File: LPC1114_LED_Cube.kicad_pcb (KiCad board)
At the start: 2 copper layers, 100 x 100 mm, 88 parts, among them Q201 BSS138, Q202 BSS138, Q203 BSS138, Q204 BSS138, Q205 IRLML6402TRPBF, Q206 IRLML6402TRPBF, Q207 IRLML6402TRPBF, Q208 IRLML6402TRPBF, Q209 BSS138, Q210 BSS138, Q211 BSS138, Q212 BSS138, Q213 IRLML6402TRPBF, Q214 IRLML6402TRPBF, Q215 IRLML6402TRPBF, Q216 IRLML6402TRPBF, Y101 12MHZ, Y102 12MHZ

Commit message: Completed Rev 1A
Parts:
- moved Q209 0.25 mm to (105.7, 74.5)
- moved Q201 0.25 mm to (90.4, 74.5)
- moved Q211 0.25 mm to (113.3, 74.5)
- moved C104 0.20 mm to (162.6, 99.9)
- moved Q212 0.13 mm to (115.1, 80.3)
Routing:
- net GND: track 92.4 -> 123.7 mm, vias 60 -> 63
- net TXD_USB: track 65.9 -> 69.3 mm
- net RXD_USB: track 65.9 -> 68.8 mm
- net LAYER_6_ON: track 63.6 -> 64.1 mm
- net Net-(LED_CH2_CTRL0-Pad27): track 7.54 -> 7.02 mm
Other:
- board text added: "0"
- board text added: "0.1uF"
- board text added: "15"
- board text added: "39pF"
- board text added: "56"
- board text added: "63"
- board text added: "7"
- board text added: "8"

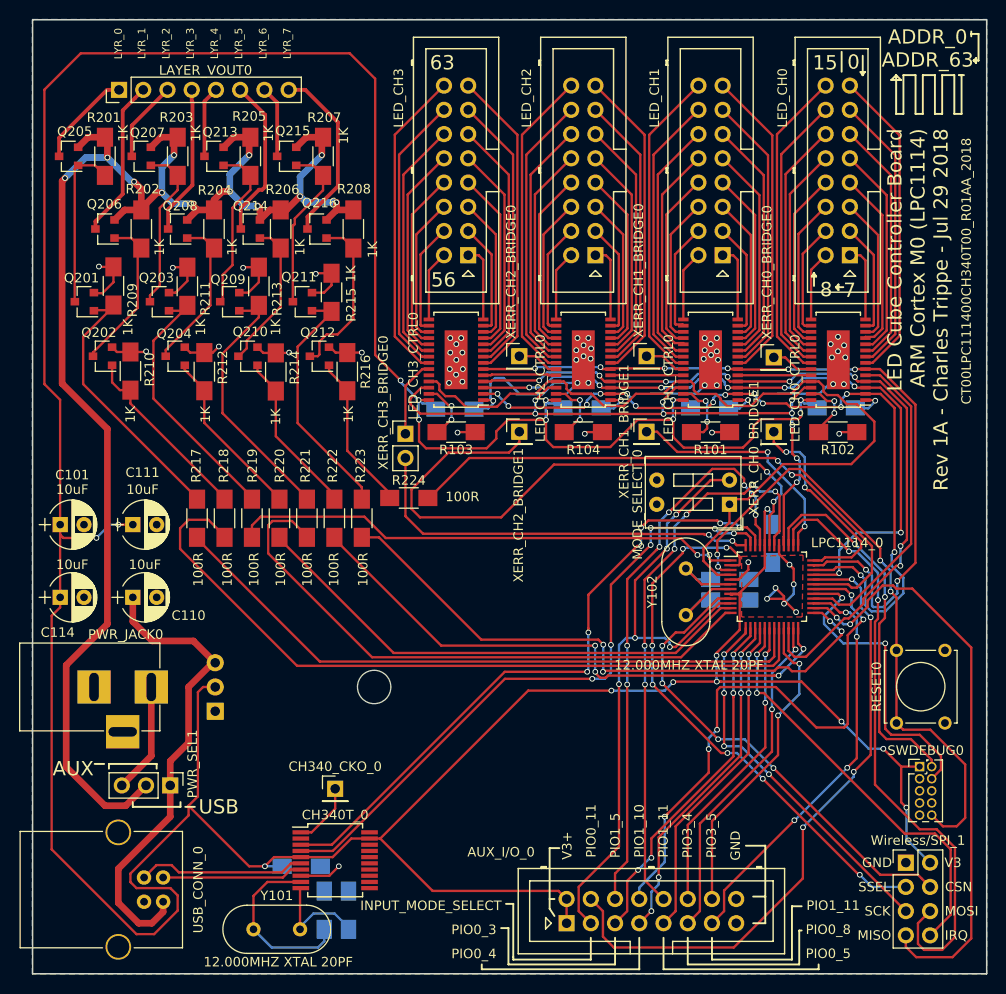
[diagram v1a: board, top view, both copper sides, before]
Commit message: Rev 1B: Corrected silkscreen component values
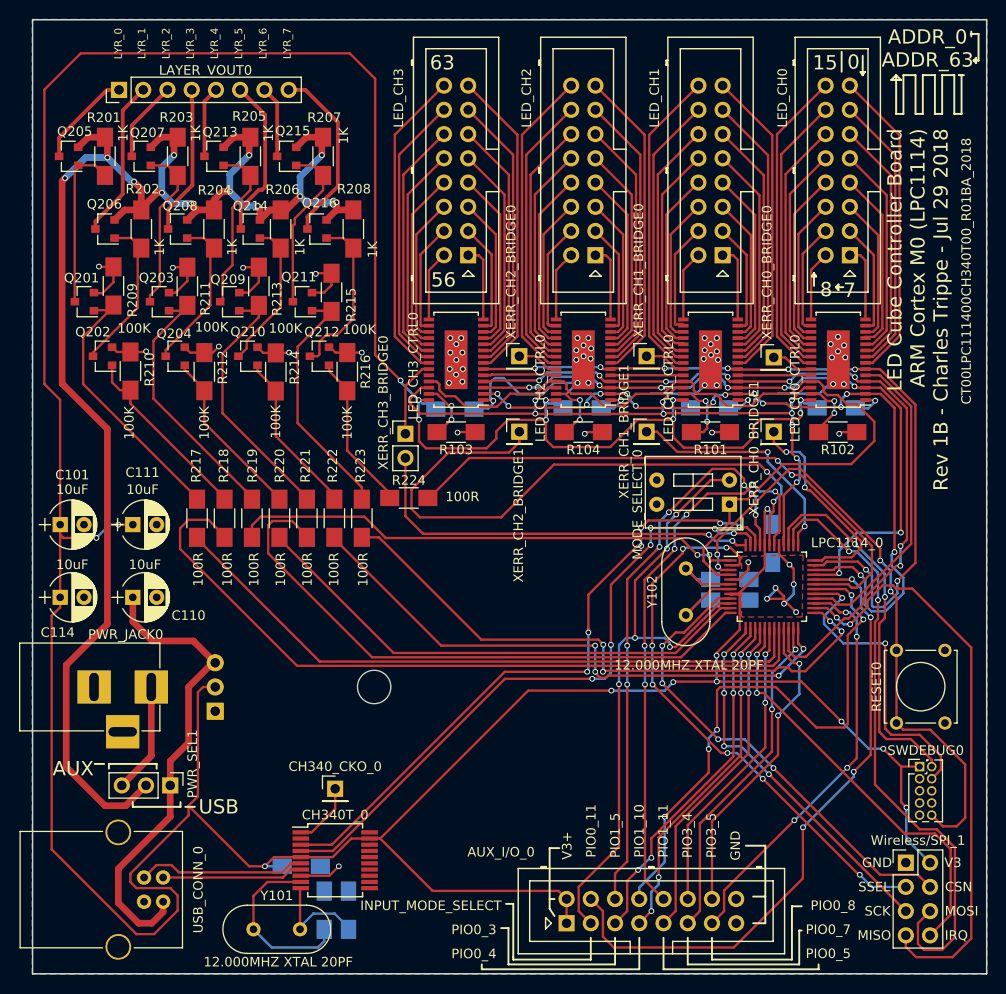
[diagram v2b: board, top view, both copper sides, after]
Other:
- board text added: "100K"
- board text added: "22pF"
- board text added: "CT00LPC111400CH340T00_R01BA_2018"
- board text added: "LED Cube Controller Board ARM Cortex M0 (LPC1114) Rev 1B - Charles Trippe - Jul 29 2018"
- board text added: "PIO0_7"
- board text removed: "CT00LPC111400CH340T00_R01AA_2018"
- board text removed: "LED Cube Controller Board ARM Cortex M0 (LPC1114) Rev 1A - Charles Trippe - Jul 29 2018"
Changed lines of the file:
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@@
   (layers
     (0 F.Cu signal)
-    (31 B.Cu signal)
+    (31 B.Cu signal hide)
     (32 B.Adhes user hide)
     (33 F.Adhes user hide)
     (34 B.Paste user hide)
     (35 F.Paste user hide)
-    (36 B.SilkS user)
+    (36 B.SilkS user hide)
     (37 F.SilkS user)
-    (38 B.Mask user)
-    (39 F.Mask user)
+    (38 B.Mask user hide)
+    (39 F.Mask user hide)
     (40 Dwgs.User user hide)
     (41 Cmts.User user hide)
@@
       (drillshape 0)
       (scaleselection 1)
-      (outputdirectory "gerber/"))
+      (outputdirectory "gerber2/"))
   )
   (net 0 "")
@@
     (tags SOT-23)
     (attr smd)
-    (fp_text reference Q202 (at 0.38354 2.48158 180) (layer F.SilkS)
+    (fp_text reference Q202 (at 1.016 2.54 180) (layer F.SilkS)
       (effects (font (size 1 1) (thickness 0.15)))
     )
@@
     (tags SOT-23)
     (attr smd)
-    (fp_text reference Q210 (at -0.2413 2.56286 180) (layer F.SilkS)
+    (fp_text reference Q210 (at 0 2.56286 180) (layer F.SilkS)
       (effects (font (size 1 1) (thickness 0.15)))
     )
@@
     (tags SOT-23)
     (attr smd)
-    (fp_text reference Q212 (at 0.1778 2.48158 180) (layer F.SilkS)
+    (fp_text reference Q212 (at -0.254 2.54 180) (layer F.SilkS)
       (effects (font (size 1 1) (thickness 0.15)))
     )
@@
     )
   )
+  (gr_text 100K (at 119.253 77.47) (layer F.SilkS)
+    (effects (font (size 1 1) (thickness 0.2)))
+  )
+  (gr_text 100K (at 111.506 77.343) (layer F.SilkS)
+    (effects (font (size 1 1) (thickness 0.2)))
+  )
+  (gr_text 100K (at 103.759 77.216) (layer F.SilkS)
+    (effects (font (size 1 1) (thickness 0.2)))
+  )
+  (gr_text 100K (at 95.631 77.343) (layer F.SilkS)
+    (effects (font (size 1 1) (thickness 0.2)))
+  )
   (gr_line (start 152.273 105.029) (end 154.305 105.029) (layer B.SilkS) (width 0.2))
   (gr_line (start 152.4 104.013) (end 154.305 104.013) (layer B.SilkS) (width 0.2))
@@
     (effects (font (size 1 1) (thickness 0.2)) (justify mirror))
   )
-  (gr_text 0.1uF (at 113.284 137.16 90) (layer B.SilkS)
+  (gr_text 22pF (at 113.284 137.16 90) (layer B.SilkS)
     (effects (font (size 1 1) (thickness 0.2)) (justify mirror))
   )
@@
     (effects (font (size 1 1) (thickness 0.2)) (justify mirror))
   )
-  (gr_text 0.1uF (at 121.793 139.446 90) (layer B.SilkS)
+  (gr_text 22pF (at 121.793 139.446 90) (layer B.SilkS)
     (effects (font (size 1 1) (thickness 0.2)) (justify mirror))
   )
@@
   (gr_poly (pts (xy 154.432 81.153) (xy 154.432 77.343) (xy 157.607 77.343) (xy 157.607 81.153)) (layer B.Mask) (width 0.15))
   (gr_poly (pts (xy 167.894 81.153) (xy 167.894 77.343) (xy 171.069 77.343) (xy 171.069 81.153)) (layer B.Mask) (width 0.15))
-  (gr_text CT00LPC111400CH340T00_R01AA_2018 (at 182.88 71.345143 90) (layer F.SilkS)
+  (gr_text CT00LPC111400CH340T00_R01BA_2018 (at 182.88 71.345143 90) (layer F.SilkS)
     (effects (font (size 1 1) (thickness 0.2)))
   )
-  (gr_text "LED Cube Controller Board\nARM Cortex M0 (LPC1114)\nRev 1A - Charles Trippe - Jul 29 2018" (at 177.8 56.388 90) (layer F.SilkS)
+  (gr_text "LED Cube Controller Board\nARM Cortex M0 (LPC1114)\nRev 1B - Charles Trippe - Jul 29 2018" (at 177.8 56.388 90) (layer F.SilkS)
     (effects (font (size 1.5 1.5) (thickness 0.3)) (justify right))
   )
@@
     (effects (font (size 1 1) (thickness 0.2)))
   )
-  (gr_text 1K (at 118.364 71.628 90) (layer F.SilkS)
-    (effects (font (size 1 1) (thickness 0.2)))
-  )
-  (gr_text 1K (at 110.49 77.216 90) (layer F.SilkS)
-    (effects (font (size 1 1) (thickness 0.2)))
-  )
-  (gr_text 1K (at 102.616 77.216 90) (layer F.SilkS)
-    (effects (font (size 1 1) (thickness 0.2)))
-  )
-  (gr_text 1K (at 94.996 77.216 90) (layer F.SilkS)
-    (effects (font (size 1 1) (thickness 0.2)))
-  )
   (gr_text 1K (at 98.298 68.834 90) (layer F.SilkS)
     (effects (font (size 1 1) (thickness 0.2)))
@@
     (effects (font (size 1 1) (thickness 0.2)))
   )
-  (gr_text 1K (at 118.11 86.36 90) (layer F.SilkS)
+  (gr_text 100K (at 117.983 87.249 90) (layer F.SilkS)
     (effects (font (size 1 1) (thickness 0.2)))
   )
-  (gr_text 1K (at 110.49 86.614 90) (layer F.SilkS)
+  (gr_text 100K (at 110.49 87.122 90) (layer F.SilkS)
     (effects (font (size 1 1) (thickness 0.2)))
   )
-  (gr_text 1K (at 103.124 86.36 90) (layer F.SilkS)
+  (gr_text 100K (at 102.997 87.249 90) (layer F.SilkS)
     (effects (font (size 1 1) (thickness 0.2)))
   )
-  (gr_text 1K (at 95.25 86.36 90) (layer F.SilkS)
+  (gr_text 100K (at 95.123 87.249 90) (layer F.SilkS)
     (effects (font (size 1 1) (thickness 0.2)))
   )
@@
     (effects (font (size 1 1) (thickness 0.2)))
   )
-  (gr_text PIO0_8 (at 168.402 140.360035) (layer F.SilkS)
+  (gr_text PIO0_7 (at 168.402 140.360035) (layer F.SilkS)
     (effects (font (size 1 1) (thickness 0.2)))
   )
@@
     (effects (font (size 1 1) (thickness 0.2)))
   )
-  (gr_text PIO1_11 (at 168.91 137.838904) (layer F.SilkS)
+  (gr_text PIO0_8 (at 168.91 137.838904) (layer F.SilkS)
     (effects (font (size 1 1) (thickness 0.2)))
   )

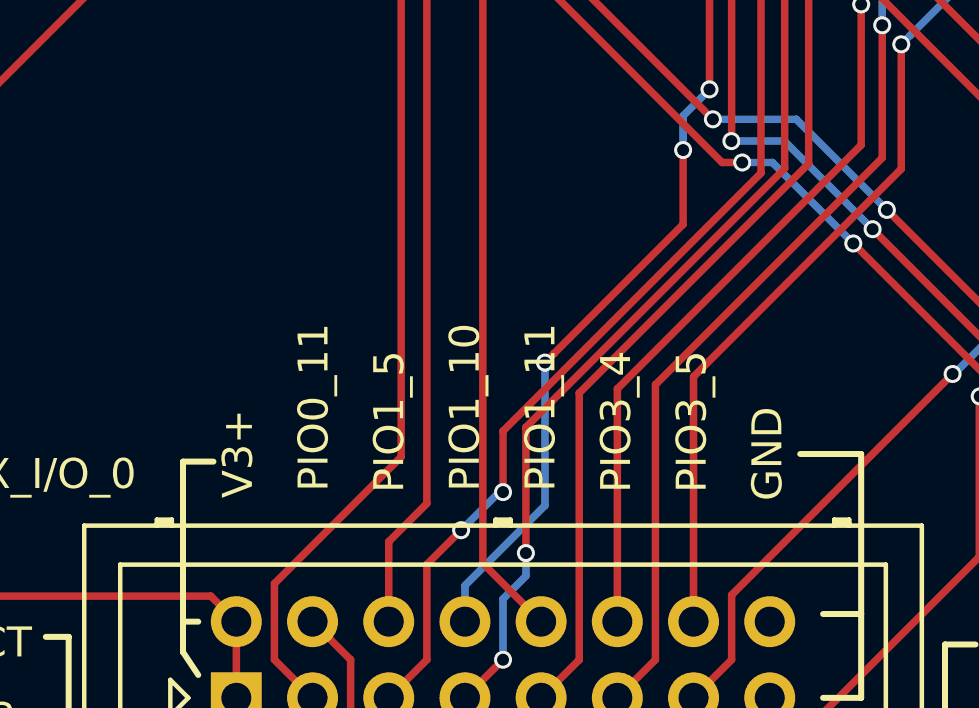
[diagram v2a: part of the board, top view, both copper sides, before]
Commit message: corrected some labeling
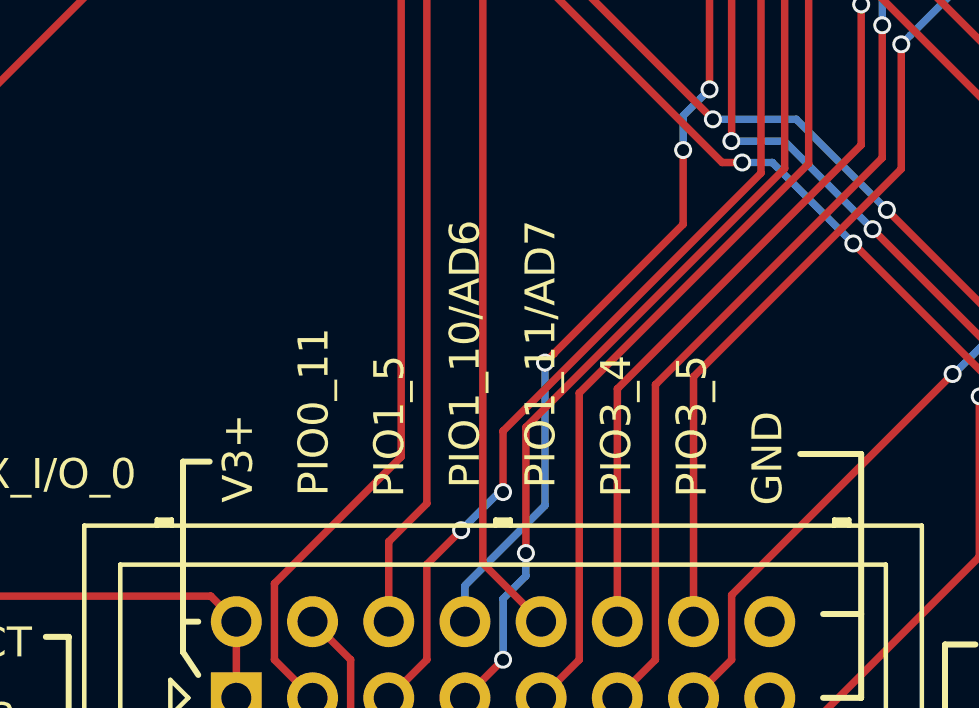
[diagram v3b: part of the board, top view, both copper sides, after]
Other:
- board text added: "PIO1_10/AD6"
- board text added: "PIO1_11/AD7"
- board text removed: "PIO1_10"
- board text removed: "PIO1_11"
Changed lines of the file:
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@@
       (drillshape 0)
       (scaleselection 1)
-      (outputdirectory "gerber2/"))
+      (outputdirectory "gerber/"))
   )
   (net 0 "")
@@
   )
   (gr_line (start 139.192 131.826) (end 139.192 138.176) (layer F.SilkS) (width 0.2))
-  (gr_line (start 140.208 131.826) (end 139.192 131.826) (layer F.SilkS) (width 0.2))
+  (gr_line (start 140.081 131.826) (end 139.192 131.826) (layer F.SilkS) (width 0.2))
   (gr_line (start 139.192 137.16) (end 139.7 137.16) (layer F.SilkS) (width 0.2))
   (gr_line (start 139.192 138.176) (end 139.7 138.938) (layer F.SilkS) (width 0.2))
@@
     (effects (font (size 1 1) (thickness 0.2)))
   )
-  (gr_text V3+ (at 141.02588 131.564426 90) (layer F.SilkS)
+  (gr_text V3+ (at 141.02588 131.714998 90) (layer F.SilkS)
     (effects (font (size 1 1) (thickness 0.2)))
   )
-  (gr_text GND (at 158.6738 131.564426 90) (layer F.SilkS)
+  (gr_text GND (at 158.6738 131.714998 90) (layer F.SilkS)
     (effects (font (size 1 1) (thickness 0.2)))
   )
-  (gr_text PIO3_5 (at 156.152666 130.492997 90) (layer F.SilkS)
+  (gr_text PIO3_5 (at 156.152666 130.643569 90) (layer F.SilkS)
     (effects (font (size 1 1) (thickness 0.2)))
   )
-  (gr_text PIO3_4 (at 153.631535 130.492997 90) (layer F.SilkS)
+  (gr_text PIO3_4 (at 153.631535 130.643569 90) (layer F.SilkS)
     (effects (font (size 1 1) (thickness 0.2)))
   )
-  (gr_text PIO1_11 (at 151.110404 130.016807 90) (layer F.SilkS)
+  (gr_text PIO1_11/AD7 (at 151.110404 128.238807 90) (layer F.SilkS)
     (effects (font (size 1 1) (thickness 0.2)))
   )
-  (gr_text PIO1_10 (at 148.589273 130.016807 90) (layer F.SilkS)
+  (gr_text PIO1_10/AD6 (at 148.589273 128.238807 90) (layer F.SilkS)
     (effects (font (size 1 1) (thickness 0.2)))
   )
-  (gr_text PIO1_5 (at 146.068142 130.492997 90) (layer F.SilkS)
+  (gr_text PIO1_5 (at 146.068142 130.643569 90) (layer F.SilkS)
     (effects (font (size 1 1) (thickness 0.2)))
   )
-  (gr_text PIO0_11 (at 143.547011 130.016807 90) (layer F.SilkS)
+  (gr_text PIO0_11 (at 143.547011 130.167379 90) (layer F.SilkS)
     (effects (font (size 1 1) (thickness 0.2)))
   )

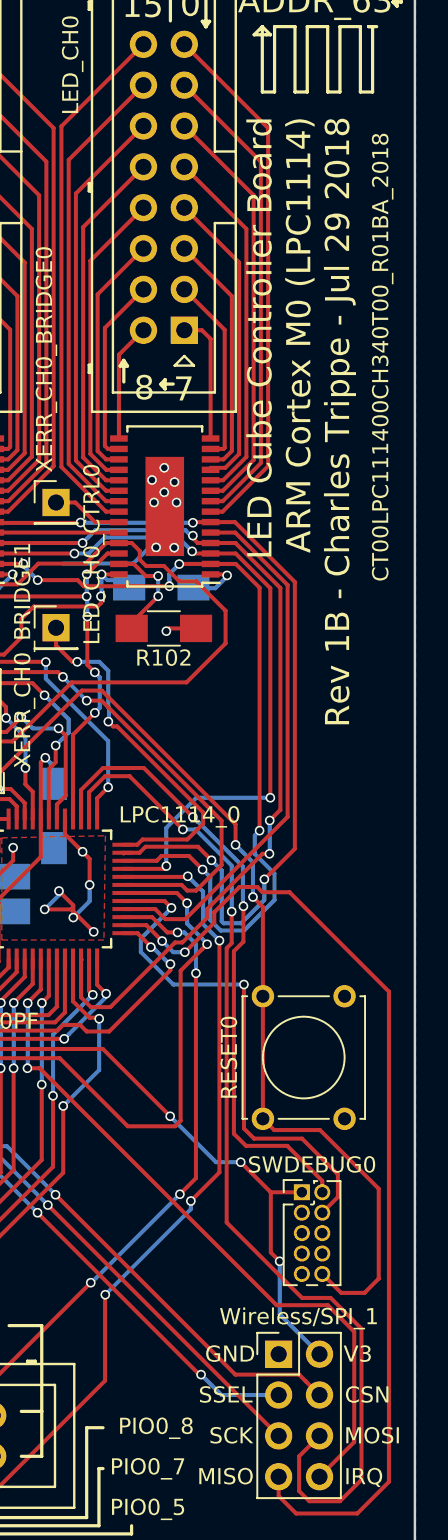
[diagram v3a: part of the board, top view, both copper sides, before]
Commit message: Text alignment
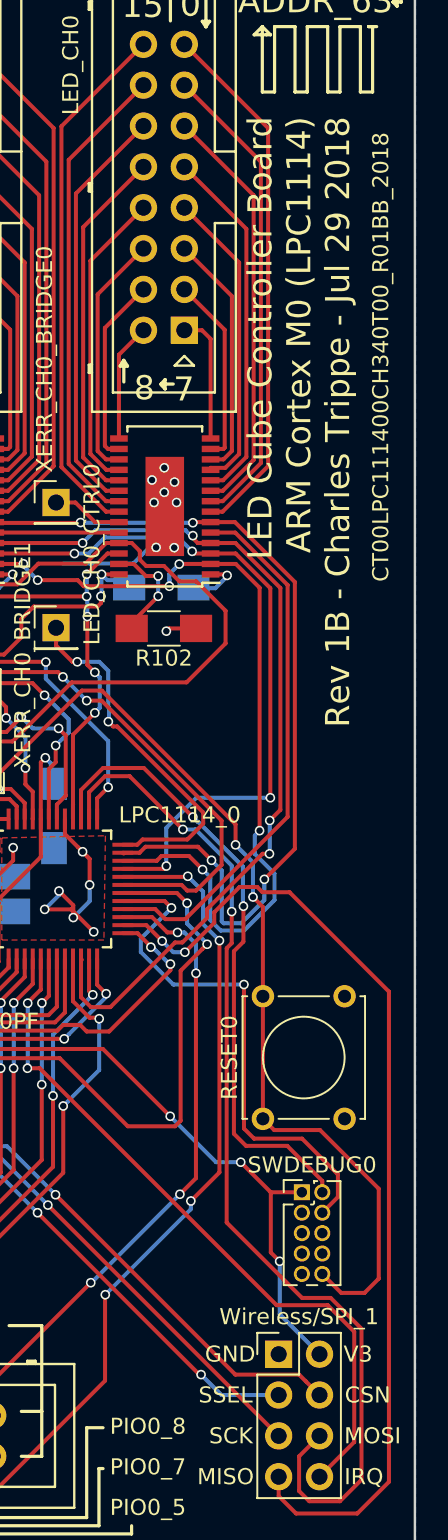
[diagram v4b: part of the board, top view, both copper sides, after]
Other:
- board text added: "CT00LPC111400CH340T00_R01BB_2018"
- board text removed: "CT00LPC111400CH340T00_R01BA_2018"
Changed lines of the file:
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@@
   (layers
     (0 F.Cu signal)
-    (31 B.Cu signal hide)
+    (31 B.Cu signal)
     (32 B.Adhes user hide)
     (33 F.Adhes user hide)
@@
   (gr_poly (pts (xy 154.432 81.153) (xy 154.432 77.343) (xy 157.607 77.343) (xy 157.607 81.153)) (layer B.Mask) (width 0.15))
   (gr_poly (pts (xy 167.894 81.153) (xy 167.894 77.343) (xy 171.069 77.343) (xy 171.069 81.153)) (layer B.Mask) (width 0.15))
-  (gr_text CT00LPC111400CH340T00_R01BA_2018 (at 182.88 71.345143 90) (layer F.SilkS)
+  (gr_text CT00LPC111400CH340T00_R01BB_2018 (at 182.88 71.345143 90) (layer F.SilkS)
     (effects (font (size 1 1) (thickness 0.2)))
   )
@@
     (effects (font (size 1 1) (thickness 0.2)))
   )
-  (gr_text PIO0_8 (at 168.91 137.838904) (layer F.SilkS)
+  (gr_text PIO0_8 (at 168.402 137.838904) (layer F.SilkS)
     (effects (font (size 1 1) (thickness 0.2)))
   )
